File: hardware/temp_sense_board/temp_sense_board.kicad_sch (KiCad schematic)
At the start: 3 parts

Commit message: Updated PCB and Schematic
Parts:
- added I2C_EXTRA1, I2C_EXTRA2, I2C_EXTRA3, I2C_EXTRA4: Conn_01x04_Socket, Connector_PinSocket_2.54mm:PinSocket_1x04_P2.54mm_Vertical, symbol Connector:Conn_01x04_Socket
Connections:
- net GND: now also I2C_EXTRA1.2 (Pin_2), I2C_EXTRA2.2 (Pin_2), I2C_EXTRA3.2 (Pin_2), I2C_EXTRA4.2 (Pin_2)
- net SCL: now also I2C_EXTRA1.3 (Pin_3), I2C_EXTRA2.3 (Pin_3), I2C_EXTRA3.3 (Pin_3), I2C_EXTRA4.3 (Pin_3)
- net SDA: now also I2C_EXTRA1.4 (Pin_4), I2C_EXTRA2.4 (Pin_4), I2C_EXTRA3.4 (Pin_4), I2C_EXTRA4.4 (Pin_4)
- net VBUS: now also I2C_EXTRA1.1 (Pin_1), I2C_EXTRA2.1 (Pin_1), I2C_EXTRA3.1 (Pin_1), I2C_EXTRA4.1 (Pin_1)

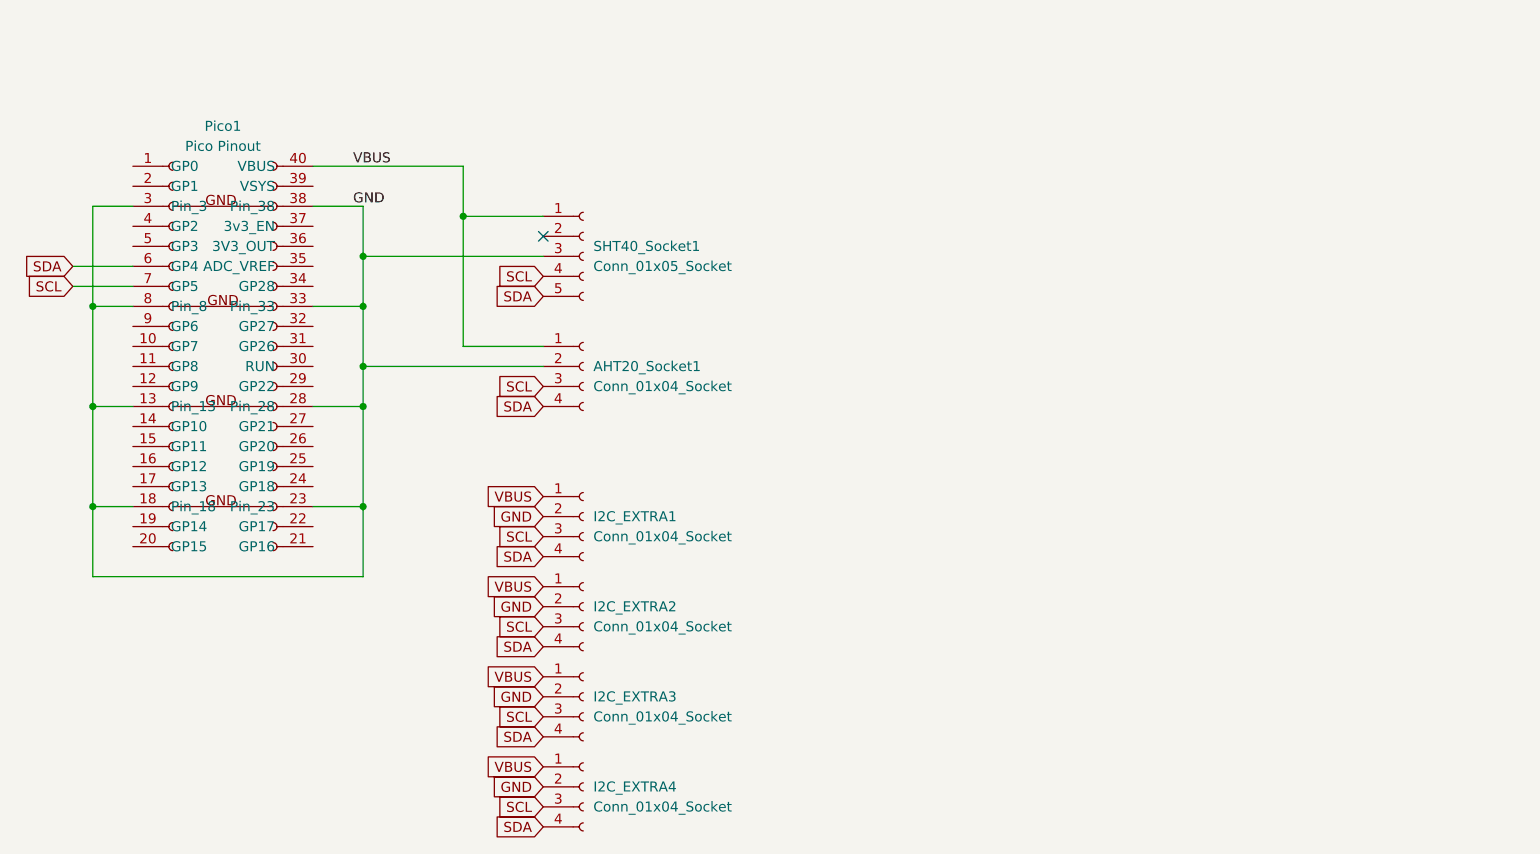
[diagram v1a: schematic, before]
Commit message: 555 timer added, not to board yet
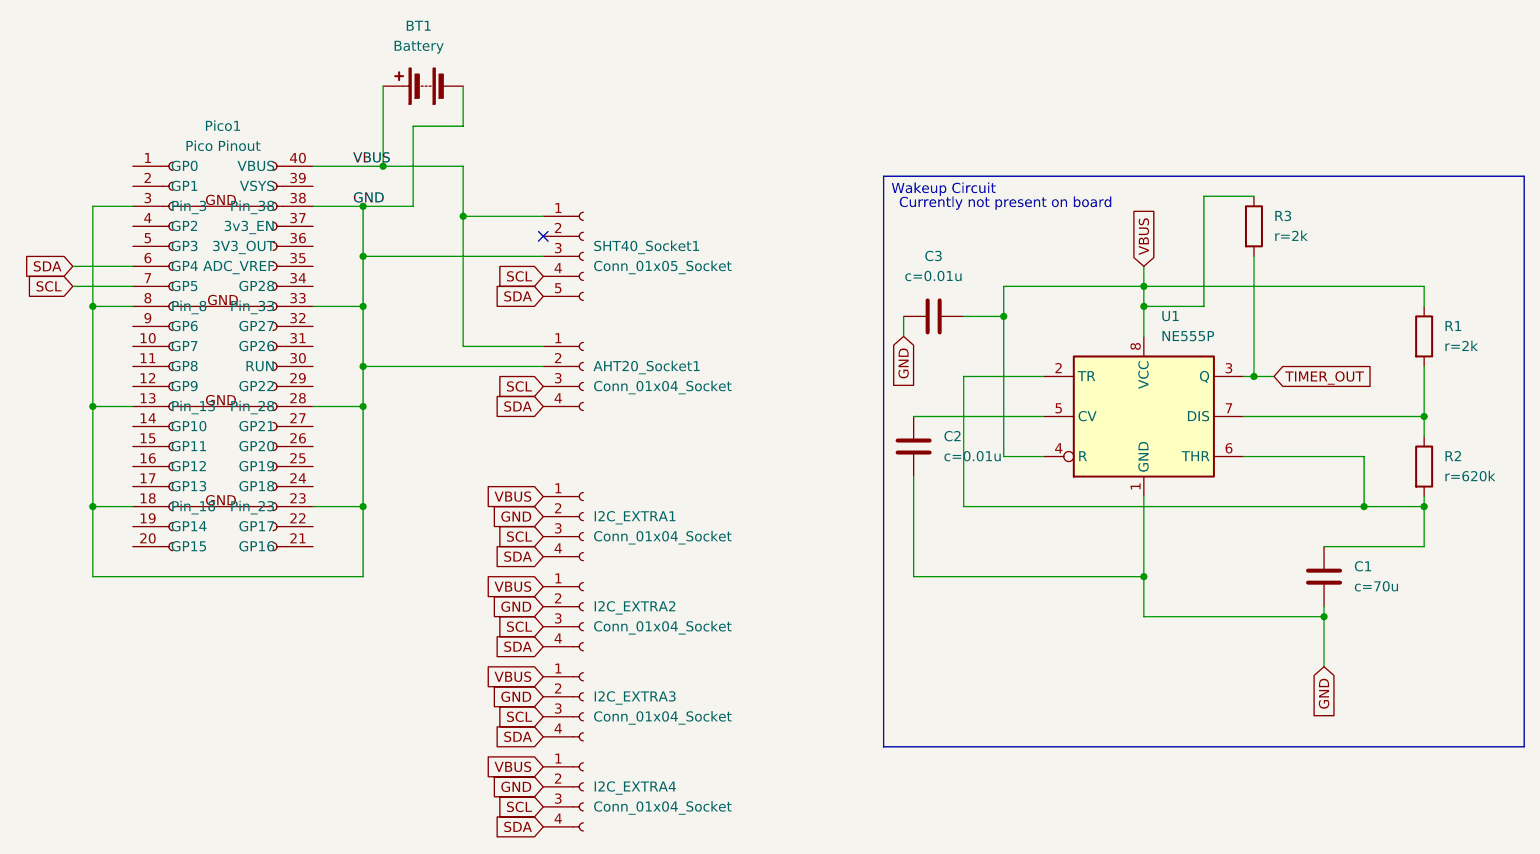
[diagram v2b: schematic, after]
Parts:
- added BT1: Battery, symbol Device:Battery
- added C1, C2, C3: ${SIM.PARAMS}, symbol Device:C
- added R1, R2, R3: ${SIM.PARAMS}, symbol Device:R
- added U1: NE555P, Package_DIP:DIP-8_W7.62mm, symbol Timer:NE555P
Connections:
- net GND: now also BT1.2 (-), C1.2, C2.2, C3.1, U1.1 (GND)
- net VBUS: now also BT1.1 (+), C3.2, R1.1, R3.1, U1.4 (R), U1.8 (VCC)
- new net: R1.2, R2.1, U1.7 (DIS)
- new net: C1.1, R2.2, U1.2 (TR), U1.6 (THR)
- new net: C2.1, U1.5 (CV)
- new net TIMER_OUT: R3.2, U1.3 (Q)
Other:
- note added: "Currently not present on board"
- note added: "Wakeup Circuit"
